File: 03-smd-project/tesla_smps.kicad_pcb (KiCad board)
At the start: 2 copper layers, 110.5 x 90.8 mm, 112 parts, among them J1 OUTPUT: 25.8 VDC/20 W, P1 Line1, P2 Line2, T1 2SK1317, T2 2N2222, T3 2N2222, U1 LTV-817, U2 LTV-817

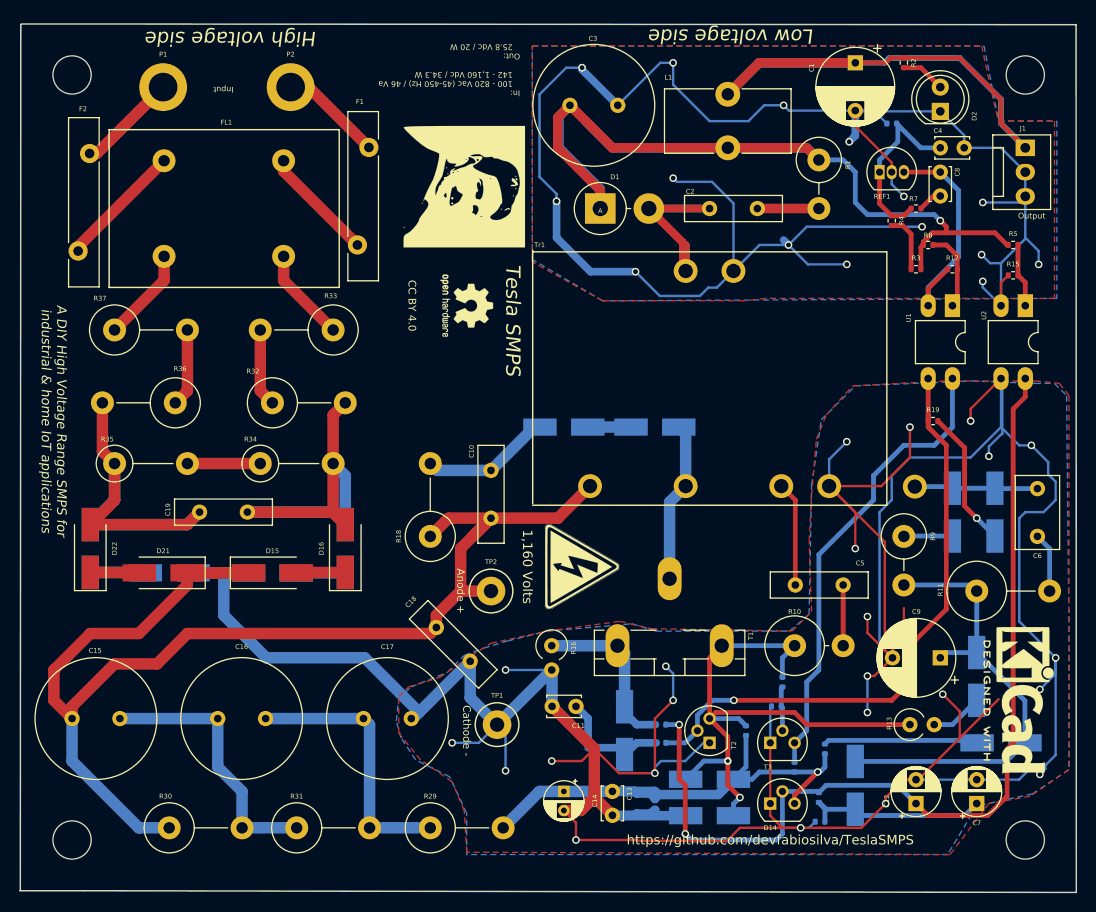
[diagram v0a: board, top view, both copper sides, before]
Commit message: Add new PCB version and changelogs
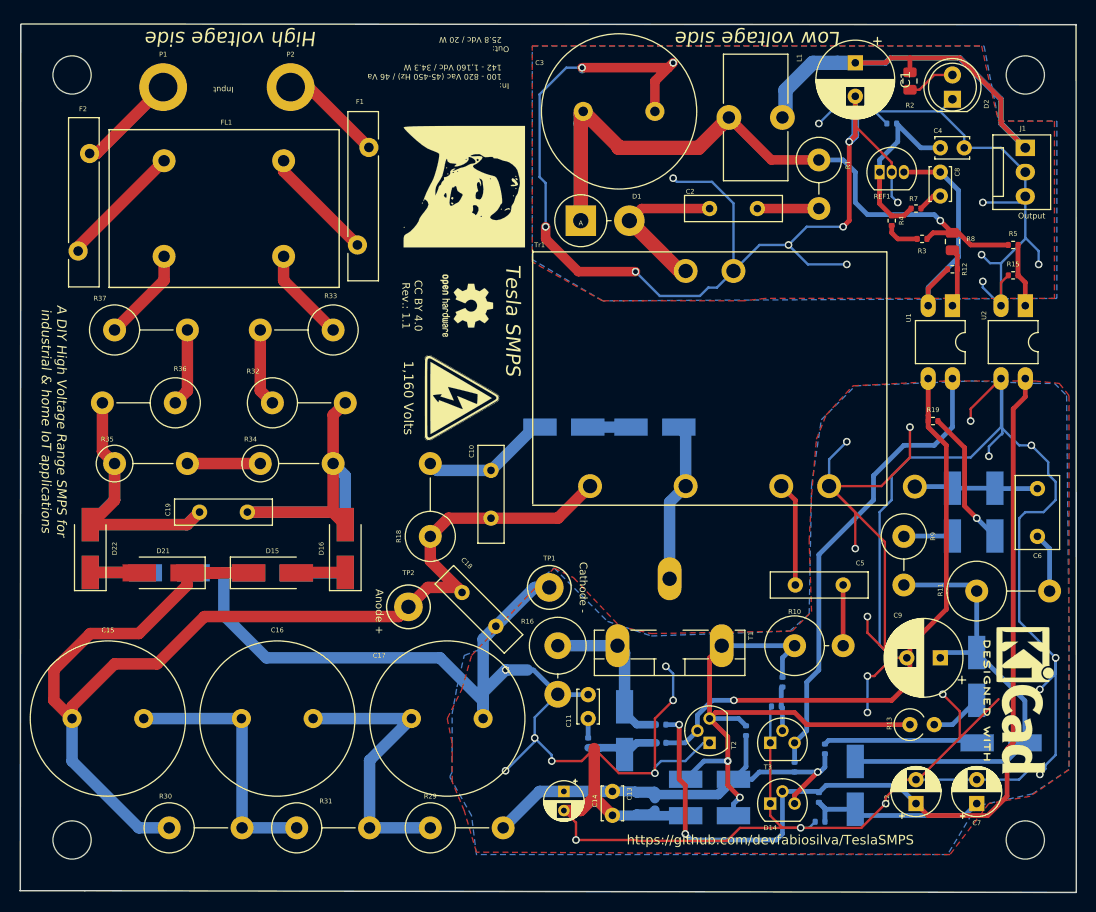
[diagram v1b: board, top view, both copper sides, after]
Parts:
- C1, C9: footprint Capacitor_THT:CP_Radial_D8.0mm_P5.00mm -> Capacitor_THT:CP_Radial_D8.0mm_P3.50mm
- C15, C16, C17: footprint Capacitor_THT:C_Radial_D12.5mm_H25.0mm_P5.00mm -> Capacitor_THT:C_Radial_D16.0mm_H31.5mm_P7.50mm
- C3: footprint Capacitor_THT:C_Radial_D12.5mm_H25.0mm_P5.00mm -> Capacitor_THT:C_Radial_D16.0mm_H25.0mm_P7.50mm
- R16: footprint Resistor_THT:R_Axial_DIN0309_L9.0mm_D3.2mm_P2.54mm_Vertical -> Resistor_THT:R_Axial_DIN0614_L14.3mm_D5.7mm_P5.08mm_Vertical
- R2, R8: footprint Resistor_SMD:R_0402_1005Metric -> Resistor_SMD:R_0805_2012Metric
- moved G*** 21.7 mm to (124.0, 98.6)
- moved TP1 15.4 mm to (133.1, 118.4)
- moved TP2 8.79 mm to (118.4, 120.4)
- moved C17 5.01 mm to (118.7, 132.1)
- moved C18 4.54 mm to (124.0, 118.9)
- moved REF** 4.23 mm to (125.5, 120.9)
- moved R3 3.24 mm to (172.1, 81.9)
- moved L1 3.18 mm to (151.9, 69.2), turned to 90 degrees
- moved R8 2.57 mm to (175.3, 82.2), turned to 90 degrees
- moved C16 2.47 mm to (100.9, 132.1)
- moved D1 2.40 mm to (136.4, 80.0)
- moved R2 2.01 mm to (170.8, 65.4)
- moved C11 1.80 mm to (137.2, 132.1), turned to 90 degrees
- moved D2 1.80 mm to (175.3, 67.3)
- moved C3 1.53 mm to (136.6, 68.6)
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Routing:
- net Net-(C2-Pad1): track 37.5 -> 18.4 mm
- net Net-(C3-Pad1): track 114.5 -> 96.9 mm
- net Net-(C1-Pad1): track 76.1 -> 59.7 mm
- net GNDPWR: track 196.9 -> 188.3 mm
- net Net-(C10-Pad1): track 132.6 -> 124.8 mm
- net Net-(R3-Pad1): track 6.08 -> 3.69 mm
- net Net-(R12-Pad2): track 8.43 -> 6.22 mm
- net Net-(C11-Pad1): track 3.83 -> 2.03 mm
- net GNDREF: track 398.4 -> 400.1 mm
- net Net-(C16-Pad2): track 28.3 -> 29.9 mm
- net Net-(C15-Pad2): track 28.4 -> 27.4 mm
- net Net-(D10-Pad2): track 17.9 -> 17.2 mm
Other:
- board text added: "CC BY 4.0 Rev.: 1.1"
- board text removed: "CC BY 4.0"

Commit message: Add release candidate for PCB version 1.1
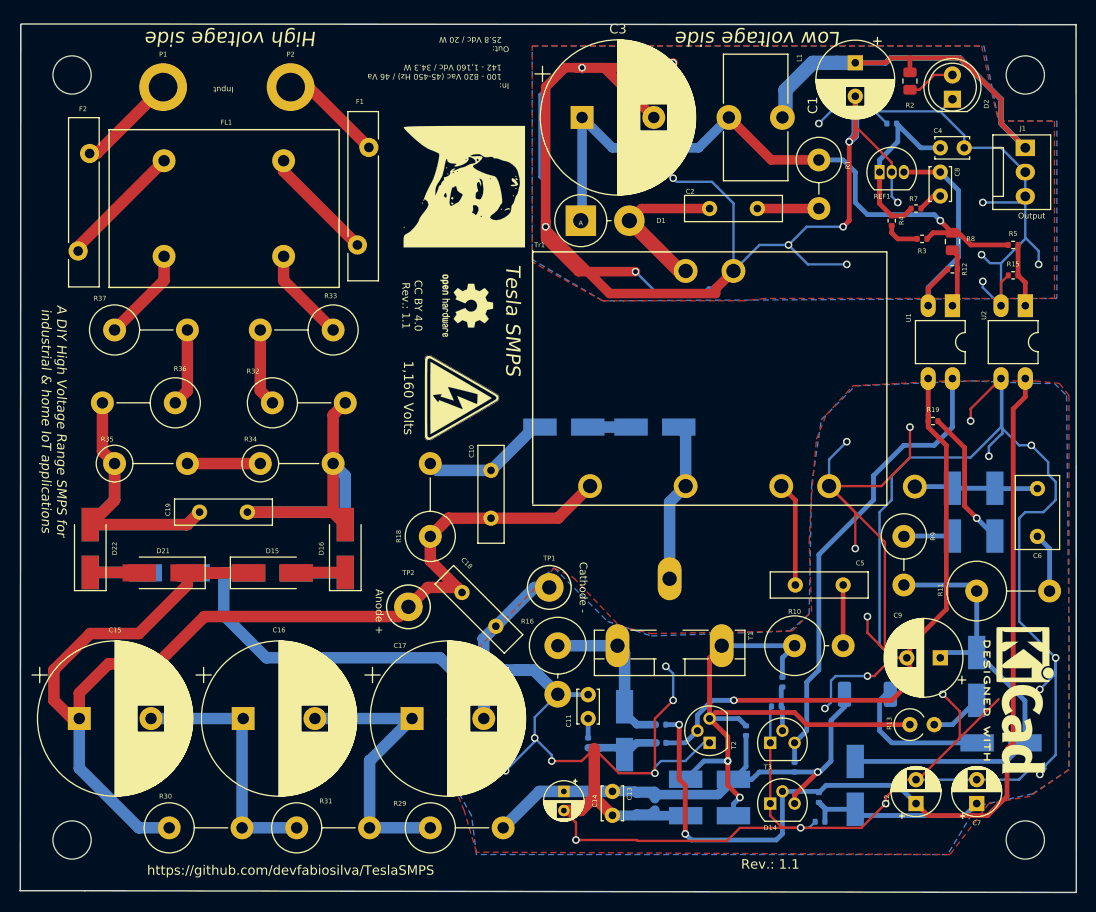
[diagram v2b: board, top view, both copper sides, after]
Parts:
- C15, C16, C17: value 47uF/450V -> CP_Radial_D16.0mm_P7.50mm; footprint Capacitor_THT:C_Radial_D16.0mm_H31.5mm_P7.50mm -> Capacitor_THT:CP_Radial_D16.0mm_P7.50mm
- C3: value 2200uF/35V -> CP_Radial_D16.0mm_P7.50mm; footprint Capacitor_THT:C_Radial_D16.0mm_H25.0mm_P7.50mm -> Capacitor_THT:CP_Radial_D16.0mm_P7.50mm
- R22: footprint Resistor_SMD:R_0402_1005Metric -> Resistor_SMD:R_2010_5025Metric_Pad1.40x2.65mm_HandSolder
- moved R22 7.24 mm to (166.4, 129.5), turned to 0 degrees
- moved C15 0.75 mm to (83.9, 132.1)
- moved C3 0.65 mm to (136.5, 69.2)
- moved C16 0.19 mm to (101.1, 132.1)
- moved C17 0.07 mm to (118.7, 132.1)
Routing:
- net GNDPWR: track 188.3 -> 238.5 mm
- net Net-(C3-Pad1): track 96.9 -> 68.7 mm
- net Net-(C13-Pad1): track 50.9 -> 58.0 mm
- net GNDREF: track 400.1 -> 402.2 mm
- net Net-(D9-Pad1): track 16.2 -> 15.7 mm
- net Net-(C10-Pad1): track 124.8 -> 125.3 mm
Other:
- board text added: "Rev.: 1.1"
